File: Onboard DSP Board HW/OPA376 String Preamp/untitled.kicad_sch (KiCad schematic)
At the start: 11 parts, among them J1 Input, U1 OPA376xxDCK

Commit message: WIP
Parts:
- U1: value OPA376xxDCK -> OPA376AIDCKT
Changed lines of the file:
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@@
 			)
 		)
-		(property "Value" "OPA376xxDCK"
+		(property "Value" "OPA376AIDCKT"
 			(at 185.674 70.104 0)
 			(show_name no)

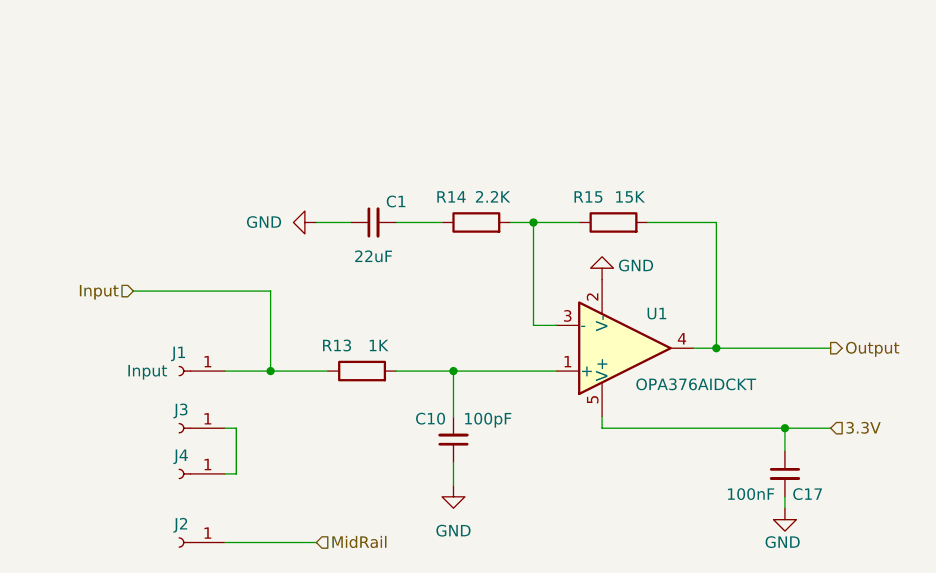
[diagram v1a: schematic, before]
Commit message: Add feedback caps damping resistors
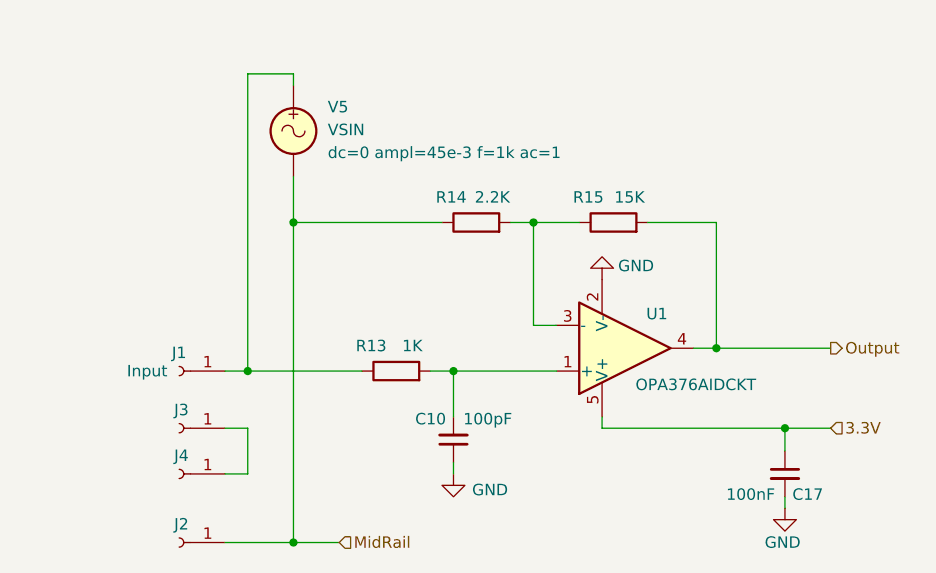
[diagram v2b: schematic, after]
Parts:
- removed C1: 22uF, Capacitor_SMD:C_0603_1608Metric, symbol Device:C_Small
- added V5: VSIN, symbol Simulation_SPICE:VSIN
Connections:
- net MidRail: now also R14.1, V5.2
- net Input: no longer names the net of J1.1 (Pin_1), R13.1
- net Input: now also V5.1
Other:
- moved on the sheet: R13

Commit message: WIP
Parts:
- added C11: 220pF, Capacitor_SMD:C_0402_1005Metric, symbol Device:C_Small
- added R25: 15k, Resistor_SMD:R_0402_1005Metric, symbol Device:R
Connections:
- net GND: now also R25.1
- net Output: now also C11.1
- net in: now reaches J1.1 (Pin_1), R13.1, V5.1
- net at C10.2, R13.2, U1.1 (+): now also R25.2
- net at R14.2, R15.1, U1.3 (-): now also C11.2
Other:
- moved on the sheet: C10, R13, V5

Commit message: preamp board modified and simulated
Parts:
- R25: value 15k -> 27K
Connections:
- net GND: no longer R25.1
- net MidRail: now also R25.1
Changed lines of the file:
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@@
+	)
+	(junction
+		(at 165.1 87.63)
+		(diameter 0)
+		(color 0 0 0 0)
 	)
 	(junction
@@
 	)
 	(junction
-		(at 140.97 87.63)
-		(diameter 0)
-		(color 0 0 0 0)
-	)
-	(junction
 		(at 167.64 52.07)
 		(diameter 0)
@@
 	)
 	(junction
+		(at 140.97 87.63)
+		(diameter 0)
+		(color 0 0 0 0)
+	)
+	(junction
 		(at 187.96 52.07)
 		(diameter 0)
@@
 	(wire
 		(pts
-			(xy 140.97 87.63) (xy 146.05 87.63)
+			(xy 140.97 87.63) (xy 165.1 87.63)
 		)
 		(stroke
@@
 	(wire
 		(pts
-			(xy 165.1 78.74) (xy 165.1 80.01)
-		)
-		(stroke
-			(width 0)
-			(type default)
-		)
-	)
-	(wire
-		(pts
 			(xy 167.64 52.07) (xy 172.72 52.07)
 		)
@@
 	(wire
 		(pts
+			(xy 165.1 78.74) (xy 165.1 87.63)
+		)
+		(stroke
+			(width 0)
+			(type default)
+		)
+	)
+	(wire
+		(pts
 			(xy 140.97 87.63) (xy 140.97 52.07)
 		)
@@
 		(pts
 			(xy 133.35 74.93) (xy 135.89 74.93)
+		)
+		(stroke
+			(width 0)
+			(type default)
+		)
+	)
+	(wire
+		(pts
+			(xy 165.1 87.63) (xy 171.45 87.63)
 		)
 		(stroke
@@
 	(hierarchical_label "MidRail"
 		(shape input)
-		(at 146.05 87.63 0)
+		(at 171.45 87.63 0)
 		(effects
 			(font
@@
 			)
 		)
-		(property "Value" "15k"
+		(property "Value" "27K"
 			(at 168.656 76.454 0)
 			(show_name no)
@@
 					(unit 1)
 				)
-			)
-		)
-	)
-	(symbol
-		(lib_id "power:GND")
-		(at 165.1 80.01 0)
-		(mirror y)
-		(unit 1)
-		(body_style 1)
-		(exclude_from_sim no)
-		(in_bom yes)
-		(on_board yes)
-		(in_pos_files yes)
-		(dnp no)
-		(property "Reference" "#PWR09"
-			(at 165.1 86.36 0)
-			(hide yes)
-			(show_name no)
-			(do_not_autoplace no)
-			(effects
-				(font
-					(size 1.27 1.27)
-				)
-			)
-		)
-		(property "Value" "GND"
-			(at 169.164 81.788 0)
-			(show_name no)
-			(do_not_autoplace no)
-			(effects
-				(font
-					(size 1.27 1.27)
-				)
-			)
-		)
-		(property "Footprint" ""
-			(at 165.1 80.01 0)
-			(hide yes)
-			(show_name no)
-			(do_not_autoplace no)
-			(effects
-				(font
-					(size 1.27 1.27)
-				)
-			)
-		)
-		(property "Datasheet" ""
-			(at 165.1 80.01 0)
-			(hide yes)
-			(show_name no)
-			(do_not_autoplace no)
-			(effects
-				(font
-					(size 1.27 1.27)
-				)
-			)
-		)
-		(property "Description" "Power symbol creates a global label with name \"GND\" , ground"
-			(at 165.1 80.01 0)
-			(hide yes)
-			(show_name no)
-			(do_not_autoplace no)
-			(effects
-				(font
-					(size 1.27 1.27)
-				)
-			)
-		)
-		(pin "1"
-		)
-		(instances
-			(project "OPA376 String Preamp"
-				(path "/02ac84b2-5c3b-408e-9eb0-8fb87f64ec2b/0e773300-e149-4e84-baf2-886502bbe02a"
-					(reference "#PWR015")
-					(unit 1)
-				)
-				(path "/02ac84b2-5c3b-408e-9eb0-8fb87f64ec2b/40966223-d92b-4fe6-9f91-9c85192c0646"
-					(reference "#PWR012")
-					(unit 1)
-				)
-				(path "/02ac84b2-5c3b-408e-9eb0-8fb87f64ec2b/5aec4146-3bdc-41db-9ec2-8493546b66d5"
-					(reference "#PWR023")
-					(unit 1)
-				)
-				(path "/02ac84b2-5c3b-408e-9eb0-8fb87f64ec2b/96d96fc6-deb5-409d-b663-ae19210fcf32"
-					(reference "#PWR09")
-					(unit 1)
-				)

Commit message: WIP
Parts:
- U1: value OPA376AIDCKT -> OPA376AIDCKR
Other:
- moved on the sheet: R25
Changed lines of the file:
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@@
 	(paper "A4")
+	(junction
+		(at 165.1 87.63)
+		(diameter 0)
+		(color 0 0 0 0)
+	)
+	(junction
+		(at 187.96 66.04)
+		(diameter 0)
+		(color 0 0 0 0)
+	)
 	(junction
 		(at 165.1 68.58)
@@
 	)
 	(junction
-		(at 165.1 87.63)
-		(diameter 0)
-		(color 0 0 0 0)
-	)
-	(junction
-		(at 187.96 66.04)
-		(diameter 0)
-		(color 0 0 0 0)
-	)
-	(junction
 		(at 167.64 52.07)
 		(diameter 0)
@@
 	(wire
 		(pts
-			(xy 165.1 68.58) (xy 165.1 71.12)
+			(xy 165.1 68.58) (xy 165.1 73.66)
 		)
 		(stroke
@@
 	(wire
 		(pts
-			(xy 165.1 78.74) (xy 165.1 87.63)
+			(xy 165.1 81.28) (xy 165.1 87.63)
 		)
 		(stroke
@@
 	(symbol
 		(lib_id "Device:R")
-		(at 165.1 74.93 180)
+		(at 165.1 77.47 180)
 		(unit 1)
 		(body_style 1)
@@
 		(dnp no)
 		(property "Reference" "R25"
-			(at 169.164 73.914 0)
+			(at 169.164 76.454 0)
 			(show_name no)
 			(do_not_autoplace no)
@@
 		)
 		(property "Value" "27K"
-			(at 168.656 76.454 0)
+			(at 168.656 78.994 0)
 			(show_name no)
 			(do_not_autoplace no)
@@
 		)
 		(property "Footprint" "Resistor_SMD:R_0402_1005Metric"
-			(at 166.878 74.93 90)
+			(at 166.878 77.47 90)
 			(hide yes)
 			(show_name no)
@@
 		)
 		(property "Datasheet" ""
-			(at 165.1 74.93 0)
+			(at 165.1 77.47 0)
 			(hide yes)
 			(show_name no)
@@
 		)
 		(property "Description" "Resistor"
-			(at 165.1 74.93 0)
+			(at 165.1 77.47 0)
 			(hide yes)
 			(show_name no)
@@
 			)
 		)
-		(property "Value" "OPA376AIDCKT"
+		(property "Value" "OPA376AIDCKR"
 			(at 185.674 70.104 0)
 			(show_name no)
